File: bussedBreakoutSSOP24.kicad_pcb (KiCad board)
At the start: 2 copper layers, 2.9 x 2.9 mm, 45 parts, among them J1 Conn_01x12_Pin, J10 Conn_01x06_Pin, J11 Conn_01x06_Pin, J12 Conn_01x06_Pin, J13 Conn_01x06_Pin, J14 Conn_01x06_Pin, J15 Conn_01x06_Pin, J16 Conn_01x06_Pin, J17 Conn_01x06_Pin, J18 Conn_01x06_Pin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

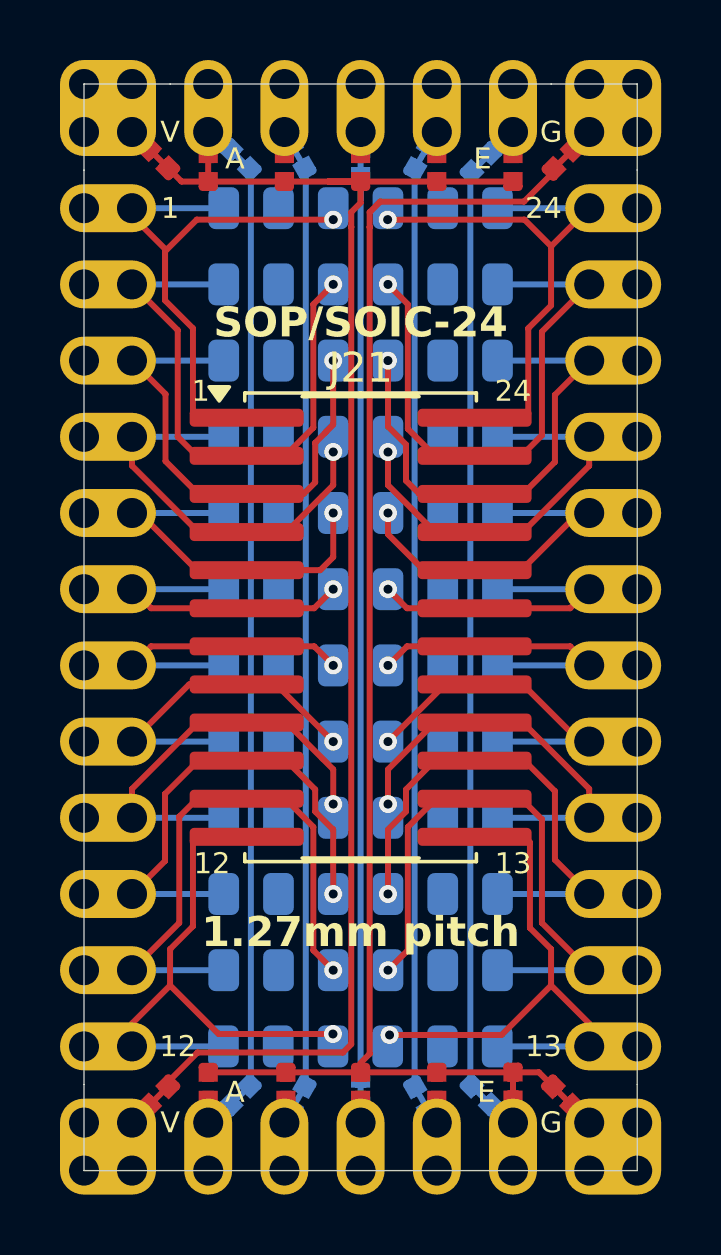
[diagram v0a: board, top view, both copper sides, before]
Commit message: Change to a SSOP-24 0.65mm pitch breakout
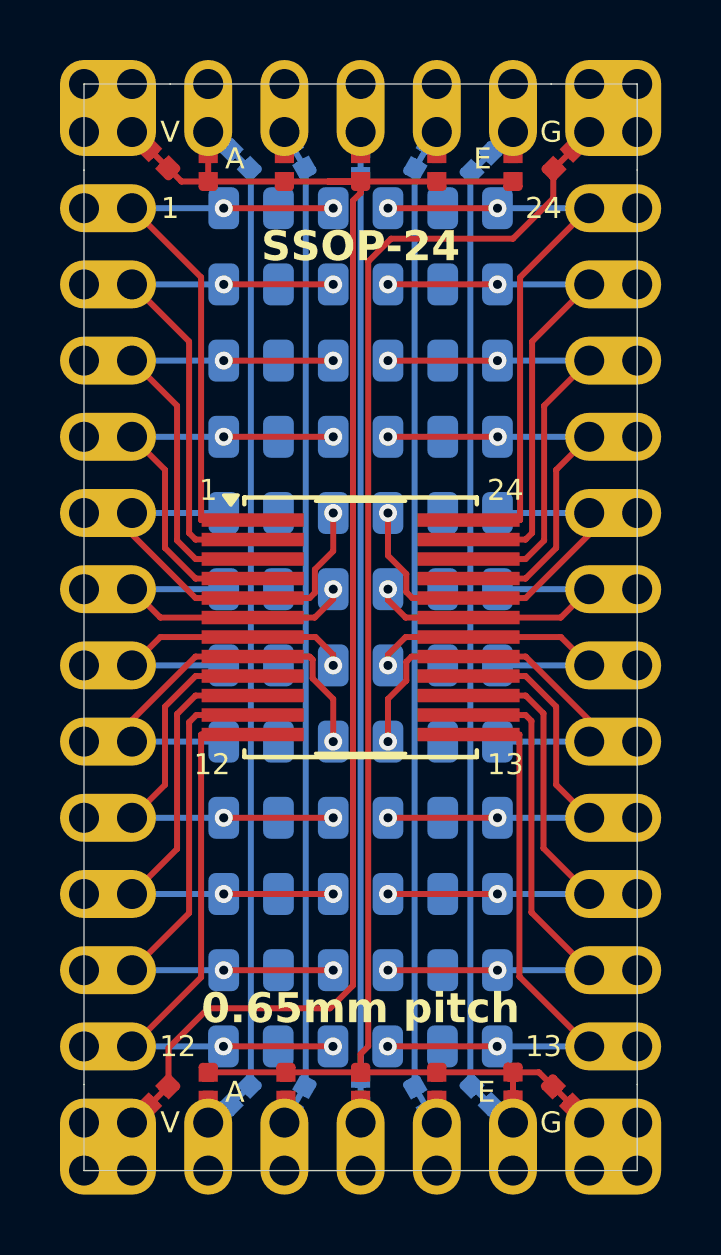
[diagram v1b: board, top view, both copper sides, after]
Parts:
- J21: value SOP-24 -> SSOP-24; footprint SMD:SOP-24_3.9-7.5mmx15.4mm_P1.27mm -> SMD:SSOP-24_3.9-7.5mmx8.2mm_P0.65mm
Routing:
- net /17: track 10.2 -> 13.7 mm
- net /8: track 10.2 -> 13.7 mm
- net /5: track 11.0 -> 14.3 mm
- net /20: track 10.6 -> 13.7 mm
- net /21: track 12.2 -> 14.2 mm, vias 1 -> 2
- net /4: track 12.2 -> 14.2 mm, vias 1 -> 2
- net /16: track 12.3 -> 14.2 mm, vias 1 -> 2
- net /9: track 12.3 -> 14.2 mm, vias 1 -> 2
- net /7: track 9.10 -> 10.8 mm
- net /19: track 9.10 -> 10.8 mm
- net /18: track 9.10 -> 10.8 mm
- net /1: track 18.4 -> 20.0 mm, vias 1 -> 2
- net /6: track 9.10 -> 10.7 mm
- net /24: track 18.4 -> 19.8 mm, vias 1 -> 2
- net /12: track 19.2 -> 20.1 mm, vias 1 -> 2
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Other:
- board text added: "0.65mm pitch"
- board text added: "SSOP-24"
- board text removed: "1.27mm pitch"
- board text removed: "SOP/SOIC-24"

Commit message: Add some prototyping area on the top
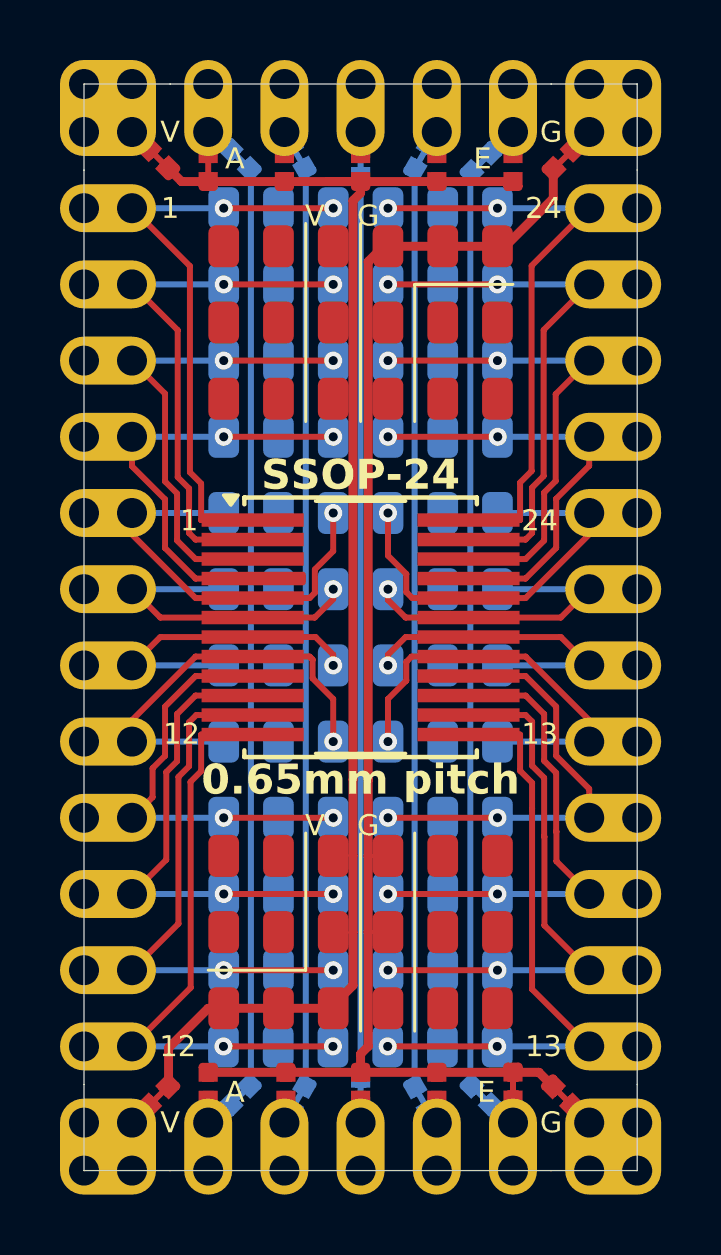
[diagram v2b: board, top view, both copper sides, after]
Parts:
- added J22: Conn_01x06_Pin, SMD:SMD_0805_grid_1x6, F.Cu at (33.0, 29.2)
- added J23: Conn_01x06_Pin, SMD:SMD_0805_grid_1x6, F.Cu at (33.0, 31.8)
- added J24: Conn_01x06_Pin, SMD:SMD_0805_grid_1x6, F.Cu at (33.0, 34.3)
- added J25: Conn_01x06_Pin, SMD:SMD_0805_grid_1x6, F.Cu at (33.0, 49.5)
- added J26: Conn_01x06_Pin, SMD:SMD_0805_grid_1x6, F.Cu at (33.0, 52.1)
- added J27: Conn_01x06_Pin, SMD:SMD_0805_grid_1x6, F.Cu at (33.0, 54.6)
